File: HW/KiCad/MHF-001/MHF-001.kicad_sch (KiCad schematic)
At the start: 204 parts, among them J1 DE15_Socket_HighDensity_Mount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, J11 PPTC081LFBN-RC, J12 M20-9980345, J2 Mini-DIN-6, J3 Conn_Coaxial, J4 PJ-102AH, J5 USB_C_Receptacle_USB2.0_16P, J6 M20-9980345, J7 M20-9980245, M3 CY7C109D-10ZXI, M5 CY7C109D-10ZXI, Q1 BC107, Q2 PMV48XP, U1 NCP1117-5.0_SOT223, U10 74HC245, U11 74HC245, U12 74HC245, U13 LMV358IDGKR, U14 LP2985-3.3, U15 ATMEGA16U2-MU, U2 74HC14, U3 74LS08, U4 74HC165, U5 ATmega2560-16A, U6 74AHC373PW, U7 74HC595, U8 74HC595, U9 74HC157, Y1 CSTNE16M0V530000R0, Y2 LFXTAL003240BULK

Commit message: +3d models, +Pins.rst, some reorganisation
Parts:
- removed C17: 22p, Capacitor_SMD:C_0603_1608Metric, symbol Device:C
- removed C18, C19: 100n, Capacitor_SMD:C_0603_1608Metric, symbol Device:C
- removed C2, C7: 47u, Arduino Mega 2560:CAP_EEHZA1E470P, symbol Device:C_Polarized
- removed D2, D5, D8: YELLOW, LED_SMD:LED_0805_2012Metric, symbol Device:LED
- removed D4: CGRB307-G, Diode_SMD:D_SMB, symbol Device:D
- removed D6: GREEN, LED_SMD:LED_0805_2012Metric, symbol Device:LED
- removed D7: CD1206-S01575, Diode_SMD:D_1206_3216Metric, symbol Device:D
- removed F1: MF-MSMF050-2, Fuse:Fuse_1812_4532Metric_Pad1.30x3.40mm_HandSolder, symbol Device:Fuse
- removed FB1, FB2: 1kΩ@100MHz, Inductor_SMD:L_0805_2012Metric, symbol Device:FerriteBead
- removed FID1, FID2, FID3, FID4: Fiducial, Fiducial:Fiducial_1mm_Mask3mm, symbol Mechanical:Fiducial
- removed J11: PPTC081LFBN-RC, Connector_PinSocket_2.54mm:PinSocket_1x08_P2.54mm_Vertical, symbol Connector_Generic:Conn_01x08
- removed J12, J6: M20-9980345, Connector_PinHeader_2.54mm:PinHeader_2x03_P2.54mm_Vertical, symbol Connector_Generic:Conn_02x03_Odd_Even
- removed J4: PJ-102AH, Connector_BarrelJack:BarrelJack_Kycon_KLDX-0202-xC_Horizontal, symbol Connector:Barrel_Jack_Switch
- removed J5: USB_C_Receptacle_USB2.0_16P, Connector_USB:USB_C_Receptacle_GCT_USB4105-xx-A_16P_TopMnt_Horizontal, symbol Connector:USB_C_Receptacle_USB2.0_16P
- removed J7: M20-9980245, Arduino Mega 2560:CONN_M20-9980245_HRW, symbol Connector_Generic:Conn_02x02_Odd_Even
- removed JP89, JP90: SolderJumper_2_Open, Jumper:SolderJumper-2_P1.3mm_Open_Pad1.0x1.5mm, symbol Jumper:SolderJumper_2_Open
- removed Q2: PMV48XP, Package_TO_SOT_SMD:SC-59, symbol Transistor_FET:Q_PMOS_GSD
- removed RN1, RN5: 10k, Resistor_SMD:R_Array_Convex_4x0612, symbol Device:R_Pack04_Split
- removed RN2: 22R, Resistor_SMD:R_Array_Convex_4x0612, symbol Device:R_Pack04_Split
- removed RN3, RN4: 1k, Resistor_SMD:R_Array_Convex_4x0612, symbol Device:R_Pack04_Split
- removed RV1, RV2: 5pF@1MHz, Resistor_SMD:R_0603_1608Metric, symbol Device:Varistor
- removed U1: NCP1117-5.0_SOT223, Package_TO_SOT_SMD:SOT-223-3_TabPin2, symbol Regulator_Linear:NCP1117-5.0_SOT223
- removed U13: LMV358IDGKR, Package_SO:MSOP-8_3x3mm_P0.65mm, symbol Arduino Mega 2560:LMV358IDGKR
- removed U14: LP2985-3.3, Package_TO_SOT_SMD:SOT-23-5, symbol Regulator_Linear:LP2985-3.3
- removed U15: ATMEGA16U2-MU, Package_DFN_QFN:VQFN-32-1EP_5x5mm_P0.5mm_EP3.1x3.1mm, symbol Arduino Mega 2560:ATMEGA16U2-MU
- removed U5: ATmega2560-16A, Package_QFP:TQFP-100_14x14mm_P0.5mm, symbol MCU_Microchip_ATmega:ATmega2560-16A
- removed Y1: CSTNE16M0V530000R0, Crystal:Resonator_SMD_Murata_CSTxExxV-3Pin_3.0x1.1mm, symbol Device:Crystal_GND2
- added C2, C7: 100n, Capacitor_SMD:C_0603_1608Metric, symbol Device:C
- added D2: D, Diode_SMD:D_1206_3216Metric, symbol Device:D
- added F1: Polyfuse, Fuse:Fuse_1206_3216Metric_Pad1.42x1.75mm_HandSolder, symbol Device:Polyfuse
- added H1, H2, H3, H4: MountingHole, MountingHole:MountingHole_3.2mm_M3, symbol Mechanical:MountingHole
- added J5: USB_B_Micro, Connector_USB:USB_Micro-B_XKB_U254-051T-4BH83-F1S, symbol Connector:USB_B_Micro
- added J8: AVR-ISP-6, Connector_PinHeader_2.54mm:PinHeader_2x03_P2.54mm_Vertical, symbol Connector:AVR-ISP-6
- added JP89, JP90: SolderJumper_2_Bridged, Jumper:SolderJumper-2_P1.3mm_Bridged_Pad1.0x1.5mm, symbol Jumper:SolderJumper_2_Bridged
- added LED1, LED2, LED3, LED4: LED, LED_SMD:LED_0201_0603Metric, symbol Device:LED
- added R28, R36: 1k, Resistor_SMD:R_0603_1608Metric, symbol Device:R
- added R29: 1M, Resistor_SMD:R_0603_1608Metric, symbol Device:R
- added R30, R31: 22, Resistor_SMD:R_0603_1608Metric, symbol Device:R
- added R32, R33: ---, Resistor_SMD:R_0603_1608Metric, symbol Device:R
- added R34, R35: 6k8, Resistor_SMD:R_0603_1608Metric, symbol Device:R
- added R37: 10k, Resistor_SMD:R_0603_1608Metric, symbol Device:R
- added U1: ATMEGA2560-16AU, Package_QFP:TQFP-100_14x14mm_P0.5mm, symbol Arduino Mega 2560:ATMEGA2560-16AU
- added U13: CH340G, Package_SO:SOIC-16_3.9x9.9mm_P1.27mm, symbol Interface_USB:CH340G
- added U14: AMS1117-5.0, Package_TO_SOT_SMD:SOT-223-3_TabPin2, symbol Regulator_Linear:AMS1117-5.0
- added U15: AMS1117-3.3, Package_TO_SOT_SMD:SOT-223-3_TabPin2, symbol Regulator_Linear:AMS1117-3.3
- added Y1: 16 MHz, Crystal:Crystal_SMD_HC49-SD, symbol Device:Crystal
- C11: value 100n -> 10M; footprint Capacitor_SMD:C_0603_1608Metric -> Capacitor_SMD:C_1206_3216Metric
- C12, C15: value 1u -> 100n
- C16: value 22p -> 100n
- D3: value CD1206-S01575 -> D; footprint Diode_SMD:D_1206_3216Metric -> Diode_SMD:D_1210_3225Metric
- R24: value 1M -> 22; now fitted
- R25: value 5k1 -> 22
- R26: value 5k1 -> 10k
- R27: now fitted
- Y2: value LFXTAL003240BULK -> 12 MHz; footprint Crystal:Crystal_HC49-4H_Vertical -> Crystal:Crystal_SMD_HC49-SD
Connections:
- net CC2 is gone; now on net Reset: R26.2
- net CMP is gone; now on net XTAL2: C14.2
- net SIGNAL_RCA is gone; now on net Bb: R5.1, U3.1
- net USBVCC is gone; now on net +5V: C10.1
- net VCC is gone; now on net GND: C4.1
- net +3.3V: now also C16.1, U15.2 (VO); no longer C15.2
- net +5V: now also C15.1, R26.1, C7.1, D2.1 (K), F1.1, J8.2 (VCC), R32.1, R33.1, R34.2, R35.2, R36.2, U1.10 (VCC), U1.100 (AVCC), U1.31 (VCC1), U1.61 (VCC2), U1.80 (VCC3), U13.16 (VCC), U14.2 (VO), U15.3 (VI); no longer C11.1, C13.2, C9.1, D3.1 (K)
- net AREF: now also U1.98 (AREF)
- net Data: now also JP90.2 (B)
- net GND: now also C15.2, C3.1, S1.5, C2.1, C7.2, J5.5 (GND), J8.6 (GND), LED3.1 (K), LED4.1 (K), R28.1, U1.11 (GND), U1.32 (GND1), U1.62 (GND2), U1.81 (GND3), U1.99 (AGND), U13.1 (GND), U14.1 (GND), U15.1 (GND); no longer C15.1, C3.2, C4.2, C9.2, R25.1, R26.1
- net Inside: now also JP39.2 (B); no longer JP36.2 (B)
- net M8RXD: now also LED1.1 (K), R30.2, U13.3 (RXD)
- net M8TXD: now also LED2.1 (K), R31.2, U13.2 (TXD)
- net Mega_6309_data0: no longer R16.2
- net Mega_6309_data1: no longer R17.2
- net Mega_6309_data2: no longer R18.2
- net Mega_6309_data3: no longer R19.2
- net Mega_6309_data4: no longer R20.2
- net Mega_6309_data5: no longer R21.2
- net Mega_6309_data6: no longer R22.2
- net Mega_6309_data7: no longer R23.2
- net PA0: now also U1.78 ((AD0)PA0)
- net PA1: now also U1.77 ((AD1)PA1)
- net PA2: now also U1.76 ((AD2)PA2)
- net PA3: now also U1.75 ((AD3)PA3)
- net PA4: now also U1.74 ((AD4)PA4)
- net PA5: now also U1.73 ((AD5)PA5)
- net PA6: now also U1.72 ((AD6)PA6)
- net PA7: now also U1.71 ((AD7)PA7)
- net PB0: now also U1.19 ((SS/PCINT0)PB0)
- net PB1: now also U1.20 ((SCK/PCINT1)PB1)
- net PB2: now also U1.21 ((MOSI/PCINT2)PB2)
- net PB3: now also U1.22 ((MISO/PCINT3)PB3)
- net PB4: now also U1.23 ((OC2A/PCINT4)PB4)
- net PB5: now also U1.24 ((OC1A/PCINT5)PB5)
- net PB6: now also U1.25 ((OC1B/PCINT6)PB6)
- net PB7: now also U1.26 ((OC0A/OC1C/PCINT7)PB7)
- net PC0: now also U1.53 ((A8)PC0)
- net PC1: now also U1.54 ((A9)PC1)
- net PC2: now also U1.55 ((A10)PC2)
- net PC3: now also U1.56 ((A11)PC3)
- net PC4: now also U1.57 ((A12)PC4)
- net PC5: now also U1.58 ((A13)PC5)
- net PC6: now also U1.59 ((A14)PC6)
- net PC7: now also U1.60 ((A15)PC7)
- net PD0: now also R33.2, U1.43 ((SCL/INT0)PD0)
- net PD1: now also R32.2, U1.44 ((SDA/INT1)PD1)
- net PD2: now also U1.45 ((RXD1/INT2)PD2)
- net PD3: now also U1.46 ((TXD1/INT3)PD3)
- net PD4: now also U1.47 ((ICP1)PD4)
- net PD5: now also U1.48 ((XCK1)PD5)
- net PD6: now also U1.49 ((T1)PD6)
- net PD7: now also U1.50 ((T0)PD7)
- net PE0: now also U1.2 ((RXD0/PCIN8)PE0)
- net PE1: now also U1.3 ((TXD0)PE1)
- net PE2: now also U1.4 ((XCK0/AIN0)PE2)
- net PE3: now also U1.5 ((OC3A/AIN1)PE3)
- net PE4: now also U1.6 ((OC3B/INT4)PE4)
- net PE5: now also U1.7 ((OC3C/INT5)PE5)
- net PE6: now also U1.8 ((T3/INT6)PE6)
- net PE7: now also U1.9 ((CLKO/ICP3/INT7)PE7)
- net PF0: now also U1.97 ((ADC0)PF0)
- net PF1: now also U1.96 ((ADC1)PF1)
- net PF2: now also U1.95 ((ADC2)PF2)
- net PF3: now also U1.94 ((ADC3)PF3)
- net PF4: now also U1.93 ((ADC4/TCK)PF4)
- net PF5: now also U1.92 ((ADC5/TMS)PF5)
- net PF6: now also U1.91 ((ADC6/TDO)PF6)
- net PF7: now also U1.90 ((ADC7/TDI)PF7)
- net PG0: now also U1.51 ((WR)PG0); no longer M3.32 (~{OE})
- net PG1: now also U1.52 ((RD)PG1); no longer M3.5 (~{WE})
- net PG2: now also U1.70 ((ALE)PG2); no longer U6.11 (LE)
- net PG3: now also U1.28 ((TOSC2)PG3); no longer M3.10 (A16)
- net PG4: now also U1.29 ((TOSC1)PG4)
- net PG5: now also U1.1 ((OC0B)PG5)
- net PH0: now also U1.12 (PH0(RXD2))
- net PH1: now also U1.13 (PH1(TXD2))
- net PH2: now also U1.14 (PH2(XCK2))
- net PH3: now also U1.15 (PH3(OC4A))
- net PH4: now also U1.16 (PH4(OC4B))
- net PH5: now also U1.17 (PH5(OC4C))
- net PH6: now also U1.18 (PH6(OC2B))
- net PH7: now also U1.27 (PH7(T4))
- net PJ0: now also U1.63 (PJ0(RXD3/PCINT9))
- net PJ1: now also U1.64 (PJ1(TXD3/PCINT10))
- net PJ2: now also U1.65 (PJ2(XCK3/PCINT11))
- net PJ3: now also U1.66 (PJ3(PCINT12))
- net PJ4: now also U1.67 (PJ4(PCINT13))
- net PJ5: now also U1.68 (PJ5(PCINT14))
- net PJ6: now also U1.69 (PJ6(PCINT15))
- net PJ7: now also U1.79 (PJ7)
- net PK0: now also U1.89 (PK0(ADC8/PCINT16))
- net PK1: now also U1.88 (PK1(ADC9/PCINT17))
- net PK2: now also U1.87 (PK2(ADC10/PCINT18))
- net PK3: now also U1.86 (PK3(ADC11/PCINT19))
- net PK4: now also U1.85 (PK4(ADC12/PCINT20))
- net PK5: now also U1.84 (PK5(ADC13/PCINT21))
- net PK6: now also U1.83 (PK6(ADC14/PCINT22))
- net PK7: now also U1.82 (PK7(ADC15/PCINT23))
- net PL0: now also U1.35 (PL0(ICP4))
- net PL1: now also U1.36 (PL1(ICP5))
- net PL2: now also U1.37 (PL2(T5))
- net PL3: now also U1.38 (PL3(OC5A))
- net PL4: now also U1.39 (PL4(OC5B))
- net PL5: now also U1.40 (PL5(OC5C))
- net PL6: now also U1.41 (PL6)
- net PL7: now also U1.42 (PL7)
- net RD+: now also R24.1, U13.5 (UD+)
- net RD-: now also R25.1, U13.6 (UD-)
- net SCL: now also JP25.2 (B)
- net SDA: now also JP26.2 (B)
- net Shared_Address_A15: now also M5.7 (A15)
- net XTAL1: now also C13.2, R29.1, U1.33 (XTAL2), Y1.2; no longer R24.1
- net XTAL2: now also R29.2, U1.34 (XTAL1), Y1.1; no longer R24.2
- net RD: now reaches JP50.2 (B)
- net RD: now also M3.32 (~{OE})
- net Rf: now reaches JP64.2 (B)
- net Rf: now also R23.2, U9.6 (I1b)
- net MISO: now reaches JP12.2 (B)
- net MISO: now also J8.1 (MISO)
- net VGA data 3: now reaches JP44.2 (B), U4.14 (D3)
- net Gf: now reaches JP63.2 (B)
- net Gf: now also R22.2, U9.10 (I1c)
- net at R27.1, Y2.2: now also C4.2, U13.7 (XI); no longer C16.1
- net at R27.2, Y2.1: now also C3.2, U13.8 (XO)
- net Reset: now reaches C12.1
- net Reset: now also C9.1, S1.3, S1.4, D2.2 (A), J8.5 (~{RST}), U1.30 (RESET)
- net VGA data 2: now reaches JP43.2 (B), U4.13 (D2)
- net Gb: now reaches JP59.2 (B)
- net Gb: now also R18.2, U9.11 (I0c)
- net XAA16: now reaches JP52.2 (B)
- net XAA16: now also M3.10 (A16), M5.10 (A16)
- net Ib: now reaches JP57.2 (B)
- net Ib: now also R16.2, U9.2 (I0a)
- net SS: now reaches JP9.2 (B)
- net VGA data 1: now reaches JP42.2 (B), U4.12 (D1)
- net VGA data 6: now reaches JP47.2 (B), U4.5 (D6)
- net ALE: now reaches JP51.2 (B)
- net ALE: now also U6.11 (LE)
- net at D1.1 (K), R1.2, U2.4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: now also JP89.2 (B)
- net CTS: now reaches JP35.2 (B)
- net CTS: now also R37.2, U13.9 (~{CTS})
- net RX: now reaches JP34.2 (B)
- net RX: now also R30.1
- net If: now reaches JP61.2 (B)
- net If: now also R20.2, U9.3 (I1a)
- net VGA data 4: now reaches JP45.2 (B), U4.3 (D4)
- net WE: now reaches JP49.2 (B)
- net WE: now also M3.5 (~{WE})
- net VGA data 7: now reaches JP48.2 (B), U4.6 (D7)
- net TX: now reaches JP33.2 (B)
- net TX: now also R31.1
- net MOSI: now reaches JP11.2 (B)
- net MOSI: now also J8.4 (MOSI)
- net Bf: now reaches U9.13 (I1d)
- net Bf: now also JP62.2 (B), R21.2
- net Bb: now reaches U9.14 (I0d)
- net Bb: now also JP58.2 (B), R17.2
- net Rb: now reaches U9.5 (I0b)
- net Rb: now also JP60.2 (B), R19.2
- net VGA data 0: now reaches JP41.2 (B), U4.11 (D0)
- net VGA Latch: now reaches JP16.2 (B), U4.1 (~{PL})
- net VGA data 5: now reaches JP46.2 (B), U4.4 (D5)
- net SCK: now reaches JP10.2 (B)
- net SCK: now also J8.3 (SCK)
- net CC1: no longer names the net of R25.2
- net CC1: now also J5.2 (D-)
- removed net RESET: C3.1, S1.3, S1.4
- net RESET2 renamed VIN
- new net: J5.3 (D+), R24.2
- new net: C9.2, R28.2, U13.13 (~{DTR})
- new net: C2.2, U13.4 (V3)
- new net: C11.1, D3.1 (K), U14.3 (VI)
- new net: F1.2, J5.1 (VBUS)
- new net L-on: LED3.2 (A), R36.1
- new net L-rx: LED1.2 (A), R34.1
- new net L-tx: LED2.2 (A), R35.1
- new net L_13: LED4.2 (A), R37.1
- new net PS2 Clock: JP89.1 (A)
- new net PS2 Data: JP90.1 (A)
- new net RTS: JP36.2 (B), U13.14 (~{RTS})
- no-connect marks 41 -> 25
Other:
- note added: "I2C: GND VCC SDA SCL"
- note added: "Input / Output connector"
- note added: "SCL"
- note added: "SDA"
- moved on the sheet: J1, JP1, JP10, JP11, JP12, JP13, JP14, JP15, JP16, JP2, JP3, JP4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

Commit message: +Comp24 footprint
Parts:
- added H5, H6, H7, H8: MountingHole, MountingHole:MountingHole_3.2mm_M3_Pad, symbol Mechanical:MountingHole
- added J4: Conn_02x32_Odd_Even, Connector_PinSocket_2.54mm:PinSocket_2x32_P2.54mm_Vertical, symbol Connector_Generic:Conn_02x32_Odd_Even
- added J6: Conn_02x32_Odd_Even, Connector_PinHeader_2.54mm:PinHeader_2x32_P2.54mm_Vertical, symbol Connector_Generic:Conn_02x32_Odd_Even
- added R38, R39: 1k, symbol Device:R
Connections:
- net D0: now also J4.1 (Pin_1), J6.1 (Pin_1)
- net D1: now also J4.2 (Pin_2), J6.2 (Pin_2)
- net D2: now also J4.3 (Pin_3), J6.3 (Pin_3)
- net D3: now also J4.4 (Pin_4), J6.4 (Pin_4)
- net D4: now also J4.5 (Pin_5), J6.5 (Pin_5)
- net D6: now also J4.7 (Pin_7), J6.7 (Pin_7)
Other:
- note added: "ATF1504"
- note added: "Arduino"
- note added: "HD6309"
- note added: "RAM-shared"
- note added: "RAM-system"
- note added: "gate-address"
- note added: "gate-data"

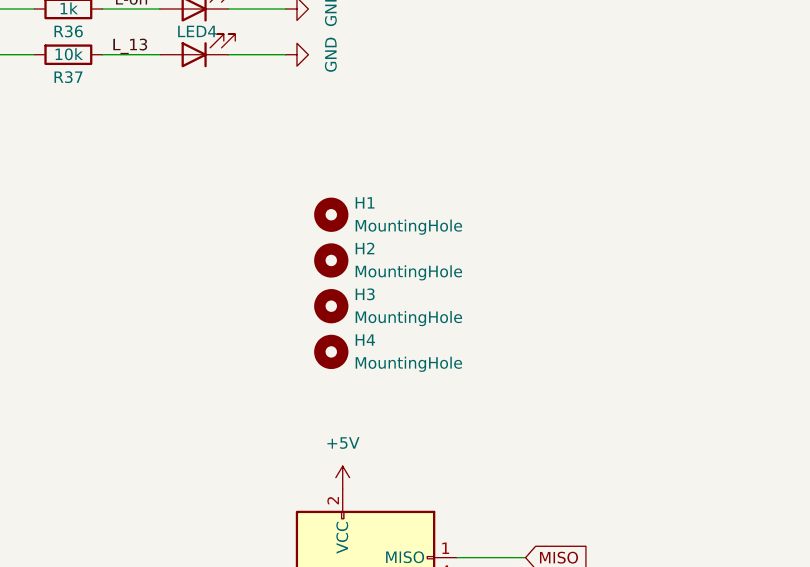
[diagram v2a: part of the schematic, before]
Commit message: - mounting holes
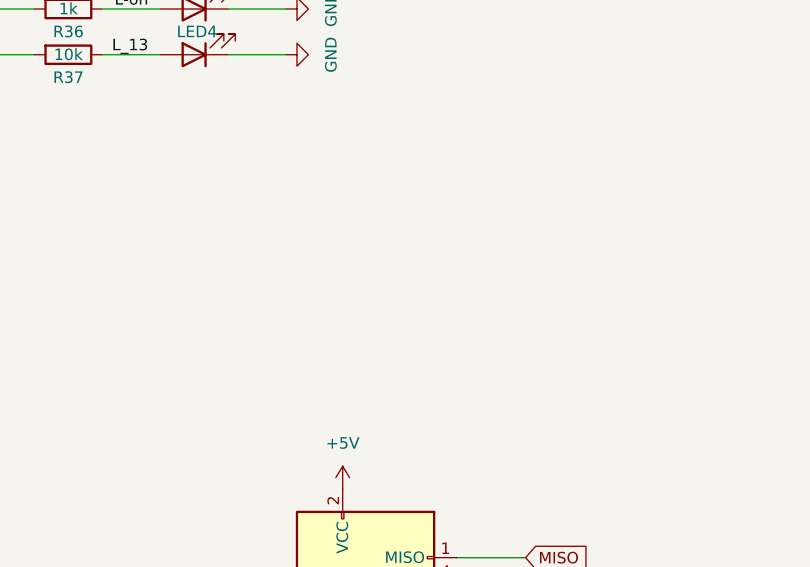
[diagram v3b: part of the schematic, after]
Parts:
- removed H1, H2, H3, H4: MountingHole, MountingHole:MountingHole_3.2mm_M3, symbol Mechanical:MountingHole

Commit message: some labels
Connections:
- net A_BUS: now also JP54.2 (B)
- net A_HALT: now also JP53.2 (B)
- net A_READ: now also JP27.2 (B)
- net A_SHARE_BUSY: now also JP32.2 (B)
- net A_SHARE_DIRTY: now also JP38.2 (B)
- net A_SHARE_GRANTED: now also JP31.2 (B)
- net A_SHARE_REQUEST: now also JP30.2 (B)
- net A_SHARE_WANTED: now also JP29.2 (B)
- net A_WRITE: now also JP28.2 (B)
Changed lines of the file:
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@@
 		)
 	)
+	(global_label "A_SHARE_WANTED"
+		(shape input)
+		(at 675.64 426.72 0)
+		(fields_autoplaced yes)
+		(effects
+			(font
+				(size 1.27 1.27)
+			)
+			(justify left)
+		)
+		(property "Intersheetrefs" "${INTERSHEET_REFS}"
+			(at 694.9537 426.72 0)
+			(effects
+				(font
+					(size 1.27 1.27)
+				)
+				(justify left)
+				(hide yes)
+			)
+		)
+	)
 	(global_label "A[0..15]"
 		(shape input)
@@
 		)
 	)
+	(global_label "A_SHARE_REQUEST"
+		(shape input)
+		(at 675.64 429.26 0)
+		(fields_autoplaced yes)
+		(effects
+			(font
+				(size 1.27 1.27)
+			)
+			(justify left)
+		)
+		(property "Intersheetrefs" "${INTERSHEET_REFS}"
+			(at 696.1027 429.26 0)
+			(effects
+				(font
+					(size 1.27 1.27)
+				)
+				(justify left)
+				(hide yes)
+			)
+		)
+	)
 	(global_label "HSyncVGA"
 		(shape input)
@@
 		)
 	)
+	(global_label "A_SHARE_GRANTED"
+		(shape input)
+		(at 675.64 431.8 0)
+		(fields_autoplaced yes)
+		(effects
+			(font
+				(size 1.27 1.27)
+			)
+			(justify left)
+		)
+		(property "Intersheetrefs" "${INTERSHEET_REFS}"
+			(at 696.0423 431.8 0)
+			(effects
+				(font
+					(size 1.27 1.27)
+				)
+				(justify left)
+				(hide yes)
+			)
+		)
+	)
 	(global_label "PH1"
 		(shape input)
@@
 		)
 	)
+	(global_label "A_SHARE_DIRTY"
+		(shape input)
+		(at 675.64 452.12 0)
+		(fields_autoplaced yes)
+		(effects
+			(font
+				(size 1.27 1.27)
+			)
+			(justify left)
+		)
+		(property "Intersheetrefs" "${INTERSHEET_REFS}"
+			(at 692.8976 452.12 0)
+			(effects
+				(font
+					(size 1.27 1.27)
+				)
+				(justify left)
+				(hide yes)
+			)
+		)
+	)
 	(global_label "VGA data 5"
 		(shape input)
@@
 		)
 	)
+	(global_label "A_HALT"
+		(shape input)
+		(at 675.64 495.3 0)
+		(fields_autoplaced yes)
+		(effects
+			(font
+				(size 1.27 1.27)
+			)
+			(justify left)
+		)
+		(property "Intersheetrefs" "${INTERSHEET_REFS}"
+			(at 685.0962 495.3 0)
+			(effects
+				(font
+					(size 1.27 1.27)
+				)
+				(justify left)
+				(hide yes)
+			)
+		)
+	)
 	(global_label "Rf"
 		(shape input)
@@
 		)
 	)
+	(global_label "A_READ"
+		(shape input)
+		(at 675.64 421.64 0)
+		(fields_autoplaced yes)
+		(effects
+			(font
+				(size 1.27 1.27)
+			)
+			(justify left)
+		)
+		(property "Intersheetrefs" "${INTERSHEET_REFS}"
+			(at 685.459 421.64 0)
+			(effects
+				(font
+					(size 1.27 1.27)
+				)
+				(justify left)
+				(hide yes)
+			)
+		)
+	)
 	(global_label "A[0..15]"
 		(shape input)
@@
 		)
 	)
+	(global_label "A_SHARE_BUSY"
+		(shape input)
+		(at 675.64 434.34 0)
+		(fields_autoplaced yes)
+		(effects
+			(font
+				(size 1.27 1.27)
+			)
+			(justify left)
+		)
+		(property "Intersheetrefs" "${INTERSHEET_REFS}"
+			(at 692.5952 434.34 0)
+			(effects
+				(font
+					(size 1.27 1.27)
+				)
+				(justify left)
+				(hide yes)
+			)
+		)
+	)
 	(global_label "{RW,CLOCK,halt}"
 		(shape input)
@@
 		)
 	)
+	(global_label "A_WRITE"
+		(shape input)
+		(at 675.64 424.18 0)
+		(fields_autoplaced yes)
+		(effects
+			(font
+				(size 1.27 1.27)
+			)
+			(justify left)
+		)
+		(property "Intersheetrefs" "${INTERSHEET_REFS}"
+			(at 686.1242 424.18 0)
+			(effects
+				(font
+					(size 1.27 1.27)
+				)
+				(justify left)
+				(hide yes)
+			)
+		)
+	)
 	(global_label "SS"
 		(shape input)
@@
 				(hide yes)
 			)
+		)
+	)
+	(global_label "A_BUS"
+		(shape input)
+		(at 675.64 497.84 0)
+		(fields_autoplaced yes)
+		(effects
+			(font
+				(size 1.27 1.27)
+			)
+			(justify left)
+		)
+		(property "Intersheetrefs" "${INTERSHEET_REFS}"
+			(at 684.4914 497.84 0)
+			(effects
+				(font
+					(size 1.27 1.27)
+				)
+				(justify left)
+				(hide yes)
+			)

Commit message: schema MHF-001 maybe OK
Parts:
- removed sys_Addr1, sys_Addr2, sys_Data1: Conn_01x08, Connector_PinHeader_2.54mm:PinHeader_1x08_P2.54mm_Vertical, symbol Connector_Generic:Conn_01x08
- added J10: I2C, Connector_PinHeader_2.54mm:PinHeader_1x04_P2.54mm_Vertical, symbol Connector_Generic:Conn_01x04
- added J11: POWER, Connector_PinHeader_2.54mm:PinHeader_2x03_P2.54mm_Vertical, symbol Connector_Generic:Conn_02x03_Odd_Even
- added J7: SPI, Connector_PinHeader_2.54mm:PinHeader_1x06_P2.54mm_Vertical, symbol Connector_Generic:Conn_01x06
- added J9: Serial, Connector_PinHeader_2.54mm:PinHeader_1x06_P2.54mm_Vertical, symbol Connector_Generic:Conn_01x06
- added JP100, JP101, JP102, JP103, JP104, JP105, JP106, JP107, JP108, JP92, JP93, JP94, JP95, JP96, JP97, JP98, JP99: SolderJumper_3_Open, Jumper:SolderJumper-3_P1.3mm_Open_RoundedPad1.0x1.5mm, symbol Jumper:SolderJumper_3_Open
- added LED5, LED6: LED, LED_SMD:LED_0805_2012Metric, symbol Device:LED
- C10, C12, C13, C14, C15, C16, C2, C3, C4, C5, C6, C7, C8, C9: footprint Capacitor_SMD:C_0603_1608Metric -> Capacitor_SMD:C_0603_1608Metric_Pad1.08x0.95mm_HandSolder
- C11: footprint Capacitor_SMD:C_1206_3216Metric -> Capacitor_SMD:C_0603_1608Metric_Pad1.08x0.95mm_HandSolder
- J6: value Conn_02x32_Odd_Even -> 02x32
- LED1, LED2, LED3, LED4: footprint LED_SMD:LED_0201_0603Metric -> LED_SMD:LED_0805_2012Metric
- R24, R25, R26, R27, R28, R29, R30, R31, R32, R33, R34, R35, R36, R37: footprint Resistor_SMD:R_0603_1608Metric -> Resistor_SMD:R_0603_1608Metric_Pad0.98x0.95mm_HandSolder
- R38, R39: footprint (none) -> Resistor_SMD:R_0805_2012Metric_Pad1.20x1.40mm_HandSolder
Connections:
- net ~{MidRAM} is gone; now on net GND: M5.30 (~{CS1}/~{CE1})
- net ~{Read} is gone; now on net S_READ: M5.32 (~{OE})
- net ~{SUPRESS} is gone; now on net VGA data 3: U3.2
- net ~{Write} is gone; now on net S_WRITE: M5.5 (~{WE})
- net +5V: now also J4.1 (Pin_1), J4.2 (Pin_2), J6.1 (Pin_1), J6.2 (Pin_2), J10.4 (Pin_4), J7.6 (Pin_6), J9.6 (Pin_6)
- net A0: now also J4.11 (Pin_11), J6.11 (Pin_11)
- net A1: now also J4.12 (Pin_12), J6.12 (Pin_12)
- net A10: now also J4.21 (Pin_21), J6.21 (Pin_21)
- net A11: now also J4.22 (Pin_22), J6.22 (Pin_22)
- net A12: now also J4.23 (Pin_23), J6.23 (Pin_23)
- net A13: now also J4.24 (Pin_24), J6.24 (Pin_24)
- net A14: now also J4.25 (Pin_25), J6.25 (Pin_25)
- net A15: now also J4.26 (Pin_26), J6.26 (Pin_26)
- net A2: now also J4.13 (Pin_13), J6.13 (Pin_13)
- net A3: now also J4.14 (Pin_14), J6.14 (Pin_14)
- net A4: now also J4.15 (Pin_15), J6.15 (Pin_15)
- net A5: now also J4.16 (Pin_16), J6.16 (Pin_16)
- net A6: now also J4.17 (Pin_17), J6.17 (Pin_17)
- net A7: now also J4.18 (Pin_18), J6.18 (Pin_18)
- net A8: now also J4.19 (Pin_19), J6.19 (Pin_19)
- net A9: now also J4.20 (Pin_20), J6.20 (Pin_20)
- net A_BUS: now also J4.29 (Pin_29), J6.29 (Pin_29), JP93.1 (A); no longer JP54.2 (B)
- net A_HALT: now also J4.31 (Pin_31), J6.31 (Pin_31), JP94.1 (A); no longer JP53.2 (B)
- net A_READ: now also J4.33 (Pin_33), J6.33 (Pin_33), JP95.1 (A); no longer JP27.2 (B)
- net A_SHARE_BUSY: now also J4.37 (Pin_37), J6.37 (Pin_37), JP97.1 (A); no longer JP32.2 (B)
- net A_SHARE_DIRTY: now also J4.39 (Pin_39), J6.39 (Pin_39), JP98.1 (A); no longer JP38.2 (B)
- net A_SHARE_GRANTED: now also J4.41 (Pin_41), J6.41 (Pin_41), JP99.1 (A); no longer JP31.2 (B)
- net A_SHARE_REQUEST: now also J4.43 (Pin_43), J6.43 (Pin_43), JP100.1 (A); no longer JP30.2 (B)
- net A_SHARE_WANTED: now also J4.45 (Pin_45), J6.45 (Pin_45), JP101.1 (A); no longer JP29.2 (B)
- net A_WRITE: now also J4.35 (Pin_35), J6.35 (Pin_35), JP96.1 (A); no longer JP28.2 (B)
- net CTS: now also R38.2, J9.2 (Pin_2)
- net D0: now also J4.3 (Pin_3), J6.3 (Pin_3); no longer J4.1 (Pin_1), J6.1 (Pin_1)
- net D1: now also J4.4 (Pin_4), J6.4 (Pin_4); no longer J4.2 (Pin_2), J6.2 (Pin_2)
- net D2: now also J4.5 (Pin_5), J6.5 (Pin_5); no longer J4.3 (Pin_3), J6.3 (Pin_3)
- net D3: now also J4.6 (Pin_6), J6.6 (Pin_6); no longer J4.4 (Pin_4), J6.4 (Pin_4)
- net D4: now also J4.7 (Pin_7), J6.7 (Pin_7); no longer J4.5 (Pin_5), J6.5 (Pin_5)
- net D5: now also J4.8 (Pin_8), J6.8 (Pin_8)
- net D6: now also J4.9 (Pin_9), J6.9 (Pin_9); no longer J4.7 (Pin_7), J6.7 (Pin_7)
- net D7: now also J4.10 (Pin_10), J6.10 (Pin_10)
- net GND: now also J4.63 (Pin_63), J4.64 (Pin_64), J5.6 (Shield), J6.63 (Pin_63), J6.64 (Pin_64), J10.3 (Pin_3), J11.2 (Pin_2), J11.4 (Pin_4), J11.6 (Pin_6), J7.5 (Pin_5), J9.5 (Pin_5), LED5.1 (K), LED6.1 (K)
- net G_A_DIR: now also U11.1 (A->B), U12.1 (A->B), JP107.2 (C)
- net G_A_OE: now also U11.19 (CE), U12.19 (CE), JP108.2 (C)
- net G_D_DIR: now also U10.1 (A->B), JP105.2 (C)
- net G_D_OE: now also U10.19 (CE), JP106.2 (C)
- net MISO: now also J7.1 (Pin_1)
- net MOSI: now also JP56.1 (A), J7.2 (Pin_2)
- net Mega_6309_data0: now also JP41.2 (B); no longer JP81.2 (B)
- net Mega_6309_data1: now also JP42.2 (B); no longer JP82.2 (B)
- net Mega_6309_data2: now also JP43.2 (B); no longer JP83.2 (B)
- net Mega_6309_data3: now also JP44.2 (B); no longer JP84.2 (B)
- net Mega_6309_data4: now also JP45.2 (B); no longer JP85.2 (B)
- net Mega_6309_data5: now also JP46.2 (B); no longer JP86.2 (B)
- net Mega_6309_data6: now also JP47.2 (B); no longer JP87.2 (B)
- net Mega_6309_data7: now also JP48.2 (B); no longer JP88.2 (B)
- net PS2 Clock: now also JP56.2 (B)
- net PS2 Data: now also JP55.2 (B)
- net RTS: now also R39.2, J9.1 (Pin_1)
- net RX: now also J9.3 (Pin_3)
- net SCK: now also JP55.1 (A), J7.3 (Pin_3)
- net SCL: now also J10.2 (Pin_2)
- net SDA: now also J10.1 (Pin_1)
- net SS: now also J7.4 (Pin_4)
- net SYNC_RCA: now also JP85.2 (B), U4.3 (D4)
- net S_READ: now also JP103.2 (C)
- net S_WRITE: now also JP104.2 (C)
- net TX: now also J9.4 (Pin_4)
- net VGA data 0: now also JP81.2 (B); no longer JP41.2 (B)
- net VGA data 1: now also JP82.2 (B); no longer JP42.2 (B)
- net VGA data 2: now also JP83.2 (B); no longer JP43.2 (B)
- net VGA data 3: now also JP84.2 (B); no longer JP44.2 (B)
- net VGA data 5: now also JP86.2 (B); no longer JP46.2 (B)
- net VGA data 6: now also JP87.2 (B); no longer JP47.2 (B)
- net VGA data 7: now also JP88.2 (B); no longer JP48.2 (B)
- net VIN: now also J11.1 (Pin_1), J11.3 (Pin_3), J11.5 (Pin_5)
- net XAA16: no longer M5.10 (A16)
- net Shared_Address_A16: now reaches JP14.2 (B)
- net Shared_Address_A16: now also M5.10 (A16), JP92.2 (C)
- net A16: now reaches J6.27 (Pin_27)
- net A16: now also J4.27 (Pin_27), JP92.1 (A)
- net B16: now reaches J6.28 (Pin_28)
- net B16: now also J4.28 (Pin_28), JP92.3 (B)
- net B_BUS: now reaches J6.30 (Pin_30)
- net B_BUS: now also J4.30 (Pin_30), JP93.3 (B)
- net B_HALT: now reaches J6.32 (Pin_32)
- net B_HALT: now also J4.32 (Pin_32), JP94.3 (B)
- net B_READ: now reaches J6.34 (Pin_34)
- net B_READ: now also J4.34 (Pin_34), JP95.3 (B)
- net B_WRITE: now reaches J6.36 (Pin_36)
- net B_WRITE: now also J4.36 (Pin_36), JP96.3 (B)
- net B_SHARE_BUSY: now reaches J6.38 (Pin_38)
- net B_SHARE_BUSY: now also J4.38 (Pin_38), JP97.3 (B)
- net B_SHARE_DIRTY: now reaches J6.40 (Pin_40)
- net B_SHARE_DIRTY: now also J4.40 (Pin_40), JP98.3 (B)
- net B_SHARE_GRANTED: now reaches J6.42 (Pin_42)
- net B_SHARE_GRANTED: now also J4.42 (Pin_42), JP99.3 (B)
- net B_SHARE_REQUEST: now reaches J6.44 (Pin_44)
- net B_SHARE_REQUEST: now also J4.44 (Pin_44), JP100.3 (B)
- net B_SHARE_WANTED: now reaches J6.46 (Pin_46)
- net B_SHARE_WANTED: now also J4.46 (Pin_46), JP101.3 (B)
- net A_S_ENABLE: now reaches J6.47 (Pin_47)
- net A_S_ENABLE: now also J4.47 (Pin_47), JP102.1 (A)
- net B_S_ENABLE: now reaches J6.48 (Pin_48)
- net B_S_ENABLE: now also J4.48 (Pin_48), JP102.3 (B)
- net A_S_READ: now reaches J6.49 (Pin_49)
- net A_S_READ: now also J4.49 (Pin_49), JP103.1 (A)
- net B_S_READ: now reaches J6.50 (Pin_50)
- net B_S_READ: now also J4.50 (Pin_50), JP103.3 (B)
- net A_S_WRITE: now reaches J6.51 (Pin_51)
- net A_S_WRITE: now also J4.51 (Pin_51), JP104.1 (A)
- net B_S_WRITE: now reaches J6.52 (Pin_52)
- net B_S_WRITE: now also J4.52 (Pin_52), JP104.3 (B)
- net A_G_D_DIR: now reaches J6.53 (Pin_53)
- net A_G_D_DIR: now also J4.53 (Pin_53), JP105.1 (A)
- net B_G_D_DIR: now reaches J6.54 (Pin_54)
- net B_G_D_DIR: now also J4.54 (Pin_54), JP105.3 (B)
- net A_G_D_OE: now reaches J6.55 (Pin_55)
- net A_G_D_OE: now also J4.55 (Pin_55), JP106.1 (A)
- net B_G_D_OE: now reaches J6.56 (Pin_56)
- net B_G_D_OE: now also J4.56 (Pin_56), JP106.3 (B)
- net A_G_A_DIR: now reaches J6.57 (Pin_57)
- net A_G_A_DIR: now also J4.57 (Pin_57), JP107.1 (A)
- net B_G_A_DIR: now reaches J6.58 (Pin_58)
- net B_G_A_DIR: now also J4.58 (Pin_58), JP107.3 (B)
- net A_G_A_OE: now reaches J6.59 (Pin_59)
- net A_G_A_OE: now also J4.59 (Pin_59), JP108.1 (A)
- net B_G_A_OE: now reaches J6.60 (Pin_60)
- net B_G_A_OE: now also J4.60 (Pin_60), JP108.3 (B)
- net PS2-OE: now reaches U7.13 (~{OE}), U8.13 (~{OE})
- net PS2-OE: now also JP13.2 (B)
- net S_ENABLE: now reaches M5.6 (CS2/CE2)
- net S_ENABLE: now also JP102.2 (C)
- net at R38.1: now also LED5.2 (A)
- net at R39.1: now also LED6.2 (A)
- removed net VGA data 4: JP45.2 (B), U4.3 (D4)
- new net X_BUS: JP54.2 (B), JP93.2 (C)
- new net X_HALT: JP53.2 (B), JP94.2 (C)
- new net X_READ: JP27.2 (B), JP95.2 (C)
- new net X_SHARE_BUSY: JP29.2 (B), JP97.2 (C)
- new net X_SHARE_DIRTY: JP30.2 (B), JP98.2 (C)
- new net X_SHARE_GRANTED: JP31.2 (B), JP99.2 (C)
- new net X_SHARE_REQUEST: JP100.2 (C), JP32.2 (B)
- new net X_SHARE_WANTED: JP101.2 (C), JP38.2 (B)
- new net X_WRITE: JP28.2 (B), JP96.2 (C)
- no-connect marks 25 -> 26
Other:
- note removed: "ATF1504"
- note removed: "Arduino"
- note removed: "HD6309"
- note removed: "RAM-shared"
- note removed: "RAM-system"
- note removed: "gate-address"
- note removed: "gate-data"
- moved on the sheet: H5, H6, H7, H8, J1, J4, J6, JP55, JP56, R14, R15
